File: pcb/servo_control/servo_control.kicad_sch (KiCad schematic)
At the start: 43 parts, among them J1 USB_B_Micro, J10 Conn_01x03_Female, J11 Conn_01x03_Female, J12 Conn_01x03_Female, J13 Conn_01x03_Female, J14 Conn_01x03_Female, J15 Conn_01x03_Female, J16 Conn_01x03_Female, J17 Conn_01x03_Female, J18 Conn_01x03_Female, J19 Conn_01x03_Female, J2 Conn_02x03_Counter_Clockwise, J20 Conn_01x03_Female, J21 Conn_01x06_Male, J3 Conn_01x03_Female, J4 Conn_01x03_Female, J5 Conn_01x03_Female, J6 Conn_01x03_Female, J7 Conn_01x03_Female, J8 Conn_01x03_Female, J9 Conn_01x03_Female, SW1 ESP_PROG, SW2 ESP_RST, U1 ATmega2560-16A, U2 LM317_SOT-223, U3 ESP32-WROOM-32, U4 MPU-9250

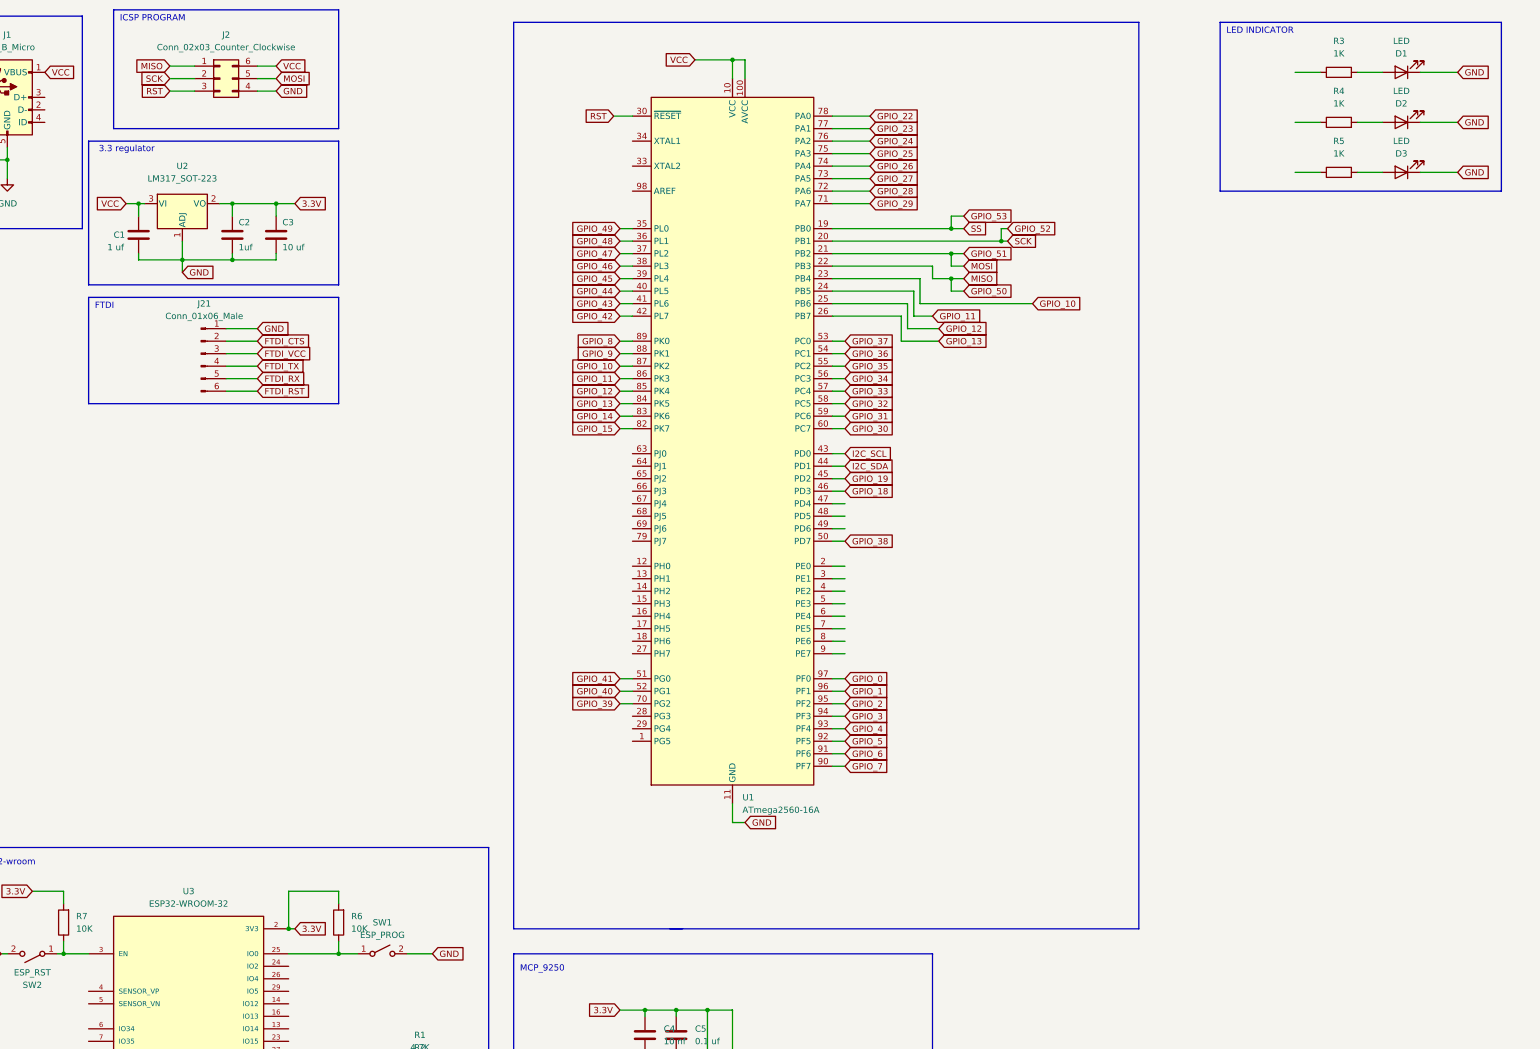
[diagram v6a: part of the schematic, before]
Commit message: change atmega2560 to PCA9685
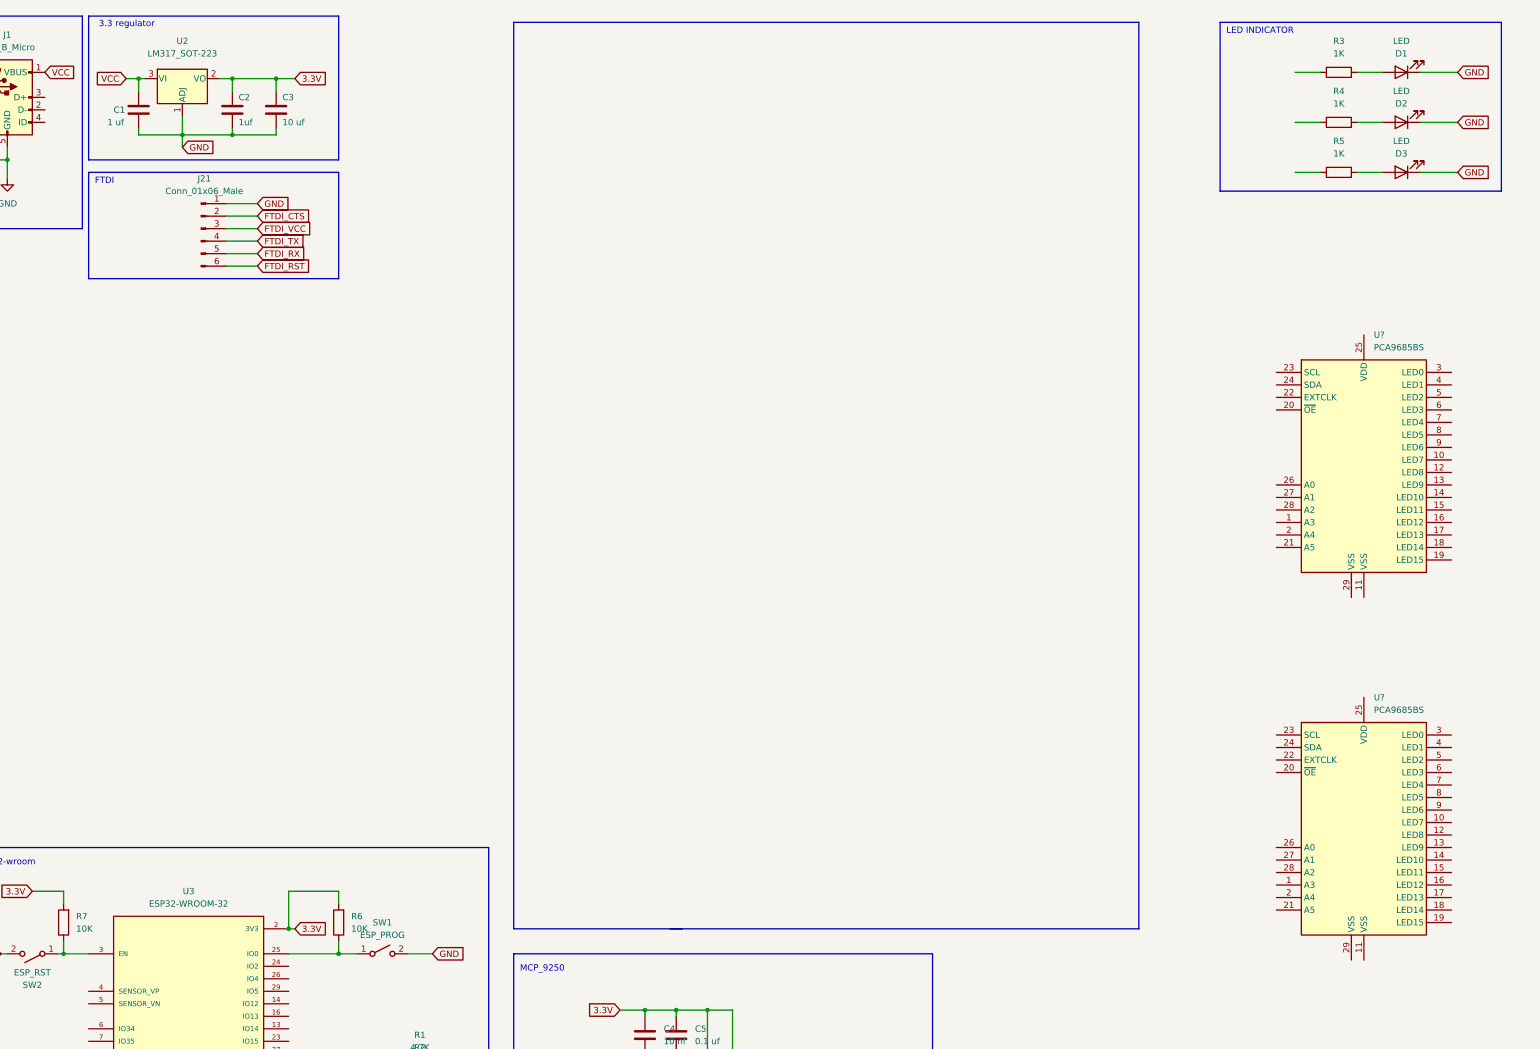
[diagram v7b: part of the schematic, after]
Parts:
- removed J2: Conn_02x03_Counter_Clockwise, Connector_PinHeader_2.54mm:PinHeader_2x03_P2.54mm_Vertical, symbol Connector_Generic:Conn_02x03_Counter_Clockwise
- removed U1: ATmega2560-16A, Package_QFP:TQFP-100_14x14mm_P0.5mm, symbol MCU_Microchip_ATmega:ATmega2560-16A
- added U? (x2): PCA9685BS, Package_DFN_QFN:QFN-28-1EP_6x6mm_P0.65mm_EP4.25x4.25mm, symbol Driver_LED:PCA9685BS
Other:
- note removed: "ICSP PROGRAM"
- moved on the sheet: C1, C2, C3, J21, U2

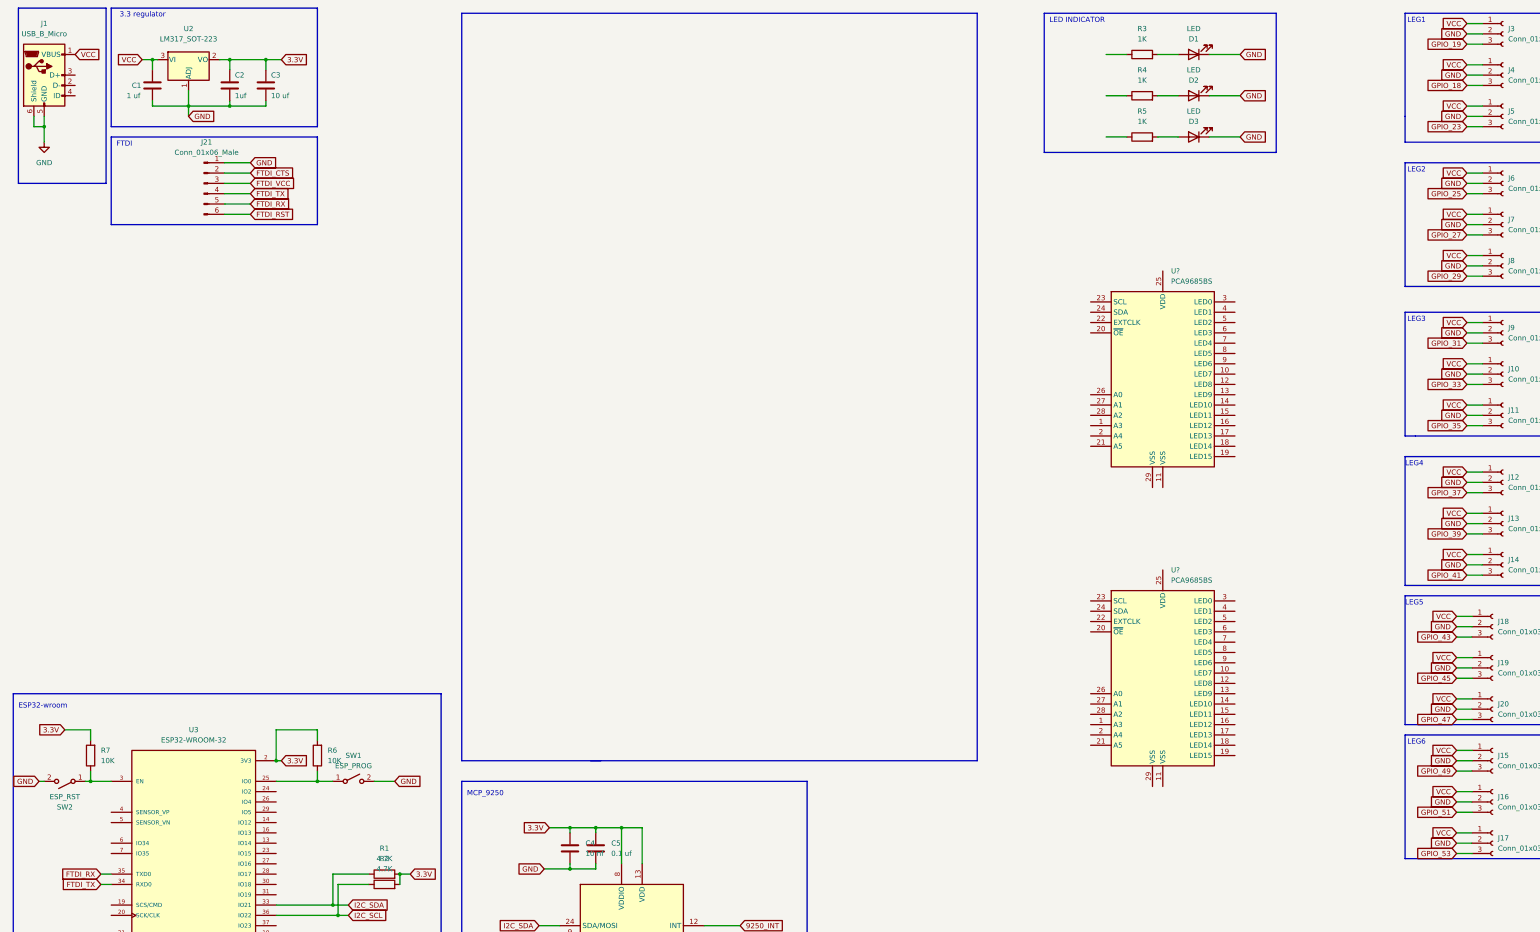
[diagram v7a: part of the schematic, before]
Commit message: wiring pcb for PCA9685
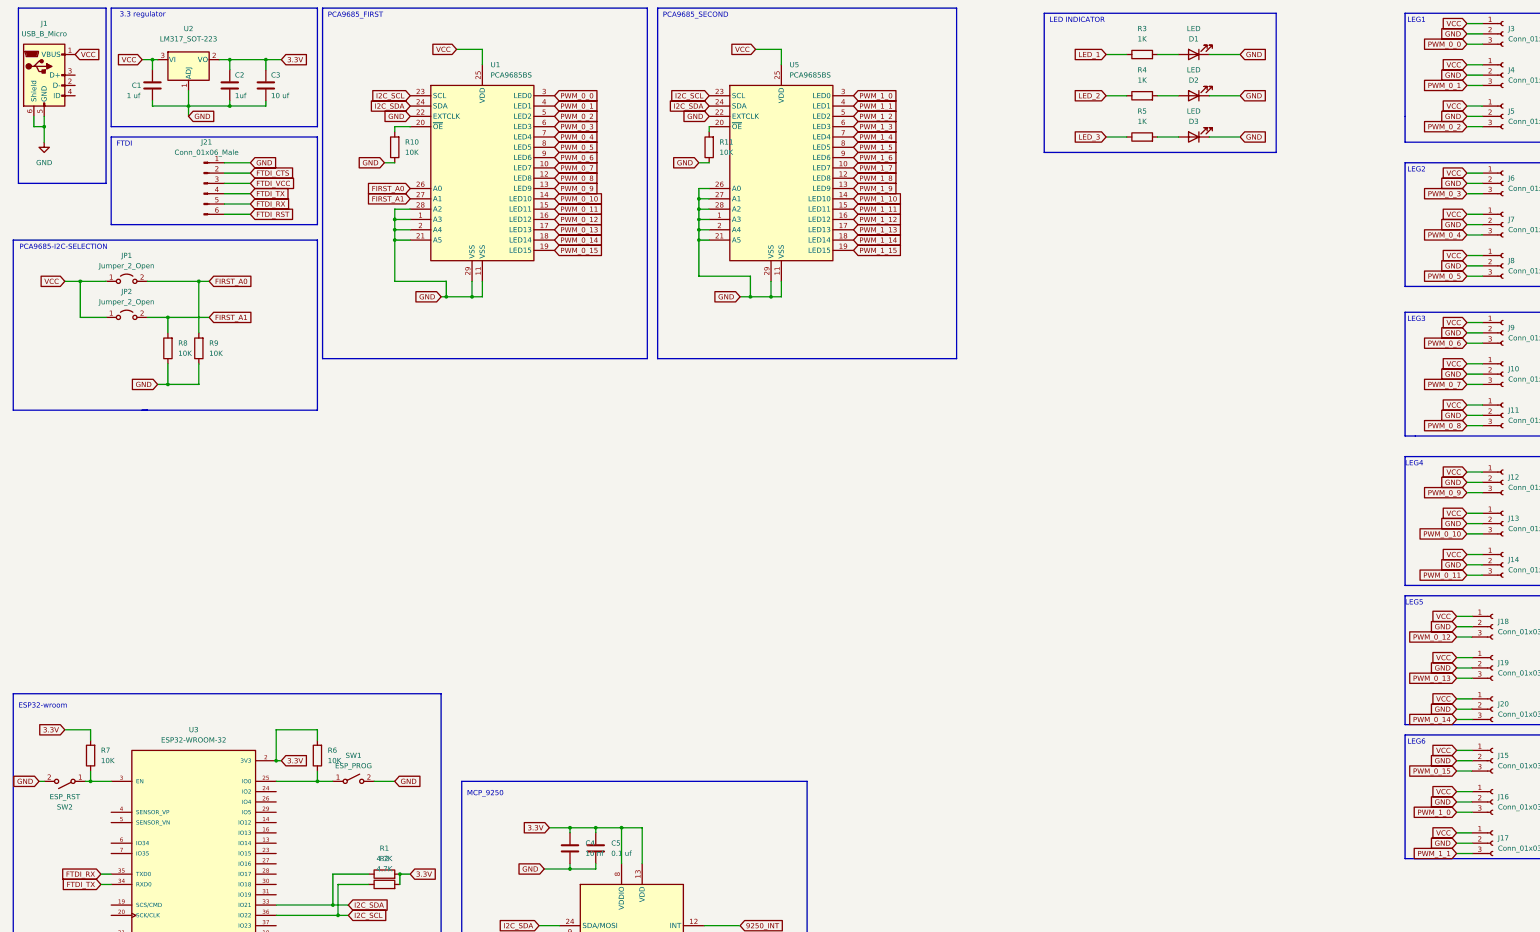
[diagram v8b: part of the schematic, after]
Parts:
- added JP1, JP2: Jumper_2_Open, Jumper:SolderJumper-2_P1.3mm_Bridged2Bar_Pad1.0x1.5mm, symbol Jumper:Jumper_2_Open
- added R10, R11, R8, R9: 10K, Resistor_SMD:R_0603_1608Metric, symbol Device:R
- U1, U5: renamed from U?; footprint Package_DFN_QFN:QFN-28-1EP_6x6mm_P0.65mm_EP4.25x4.25mm -> Package_SO:HTSSOP-28-1EP_4.4x9.7mm_P0.65mm_EP3.4x9.5mm
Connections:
- net GPIO_18 is gone; now on net PWM_0_1: J4.3 (Pin_3)
- net GPIO_19 is gone; now on net PWM_0_0: J3.3 (Pin_3)
- net GPIO_23 is gone; now on net PWM_0_2: J5.3 (Pin_3)
- net GPIO_25 is gone; now on net PWM_0_3: J6.3 (Pin_3)
- net GPIO_27 is gone; now on net PWM_0_4: J7.3 (Pin_3)
- net GPIO_29 is gone; now on net PWM_0_5: J8.3 (Pin_3)
- net GPIO_31 is gone; now on net PWM_0_6: J9.3 (Pin_3)
- net GPIO_33 is gone; now on net PWM_0_7: J10.3 (Pin_3)
- net GPIO_35 is gone; now on net PWM_0_8: J11.3 (Pin_3)
- net GPIO_37 is gone; now on net PWM_0_9: J12.3 (Pin_3)
- net GPIO_39 is gone; now on net PWM_0_10: J13.3 (Pin_3)
- net GPIO_41 is gone; now on net PWM_0_11: J14.3 (Pin_3)
- net GPIO_43 is gone; now on net PWM_0_12: J18.3 (Pin_3)
- net GPIO_45 is gone; now on net PWM_0_13: J19.3 (Pin_3)
- net GPIO_47 is gone; now on net PWM_0_14: J20.3 (Pin_3)
- net GPIO_49 is gone; now on net PWM_0_15: J15.3 (Pin_3)
- net GPIO_51 is gone; now on net PWM_1_0: J16.3 (Pin_3)
- net GPIO_53 is gone; now on net PWM_1_1: J17.3 (Pin_3)
- net GND: now also U1.1 (A3), U1.11 (VSS), U1.2 (A4), U1.21 (A5), U1.22 (EXTCLK), U1.28 (A2), U1.29 (VSS), U5.1 (A3), U5.11 (VSS), U5.2 (A4), U5.21 (A5), U5.22 (EXTCLK), U5.26 (A0), U5.27 (A1), U5.28 (A2), U5.29 (VSS), R10.1, R11.1, R8.1, R9.1
- net I2C_SCL: now also U1.23 (SCL), U5.23 (SCL)
- net I2C_SDA: now also U1.24 (SDA), U5.24 (SDA)
- net VCC: now also U1.25 (VDD), U5.25 (VDD), JP1.1 (A), JP2.1 (A)
- net LED_3: now reaches R5.1
- net PWM_1_7: now reaches U5.10 (LED7)
- net PWM_1_8: now reaches U5.12 (LED8)
- net PWM_1_9: now reaches U5.13 (LED9)
- net PWM_1_10: now reaches U5.14 (LED10)
- net PWM_1_11: now reaches U5.15 (LED11)
- net PWM_1_12: now reaches U5.16 (LED12)
- net PWM_1_13: now reaches U5.17 (LED13)
- net PWM_1_14: now reaches U5.18 (LED14)
- net PWM_1_15: now reaches U5.19 (LED15)
- net at U5.20 (~{OE}): now also R11.2
- net PWM_1_0: now reaches U5.3 (LED0)
- net PWM_1_1: now reaches U5.4 (LED1)
- net PWM_1_2: now reaches U5.5 (LED2)
- net PWM_1_3: now reaches U5.6 (LED3)
- net PWM_1_4: now reaches U5.7 (LED4)
- net PWM_1_5: now reaches U5.8 (LED5)
- net PWM_1_6: now reaches U5.9 (LED6)
- net PWM_0_7: now reaches U1.10 (LED7)
- net PWM_0_8: now reaches U1.12 (LED8)
- net PWM_0_9: now reaches U1.13 (LED9)
- net PWM_0_10: now reaches U1.14 (LED10)
- net PWM_0_11: now reaches U1.15 (LED11)
- net PWM_0_12: now reaches U1.16 (LED12)
- net PWM_0_13: now reaches U1.17 (LED13)
- net PWM_0_14: now reaches U1.18 (LED14)
- net PWM_0_15: now reaches U1.19 (LED15)
- net at U1.20 (~{OE}): now also R10.2
- net FIRST_A0: now reaches U1.26 (A0)
- net FIRST_A0: now also JP1.2 (B), R9.2
- net FIRST_A1: now reaches U1.27 (A1)
- net FIRST_A1: now also JP2.2 (B), R8.2
- net PWM_0_0: now reaches U1.3 (LED0)
- net PWM_0_1: now reaches U1.4 (LED1)
- net PWM_0_2: now reaches U1.5 (LED2)
- net PWM_0_3: now reaches U1.6 (LED3)
- net PWM_0_4: now reaches U1.7 (LED4)
- net PWM_0_5: now reaches U1.8 (LED5)
- net PWM_0_6: now reaches U1.9 (LED6)
- net LED_1: now reaches R3.1
- net LED_2: now reaches R4.1
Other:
- note added: "PCA9685-I2C-SELECTION"
- note added: "PCA9685_FIRST"
- note added: "PCA9685_SECOND"
- moved on the sheet: U1, U5
